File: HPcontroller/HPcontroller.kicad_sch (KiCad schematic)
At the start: 8 parts, among them J5 54-00174, U7 Adafruit_QTPY_ESP32-C3

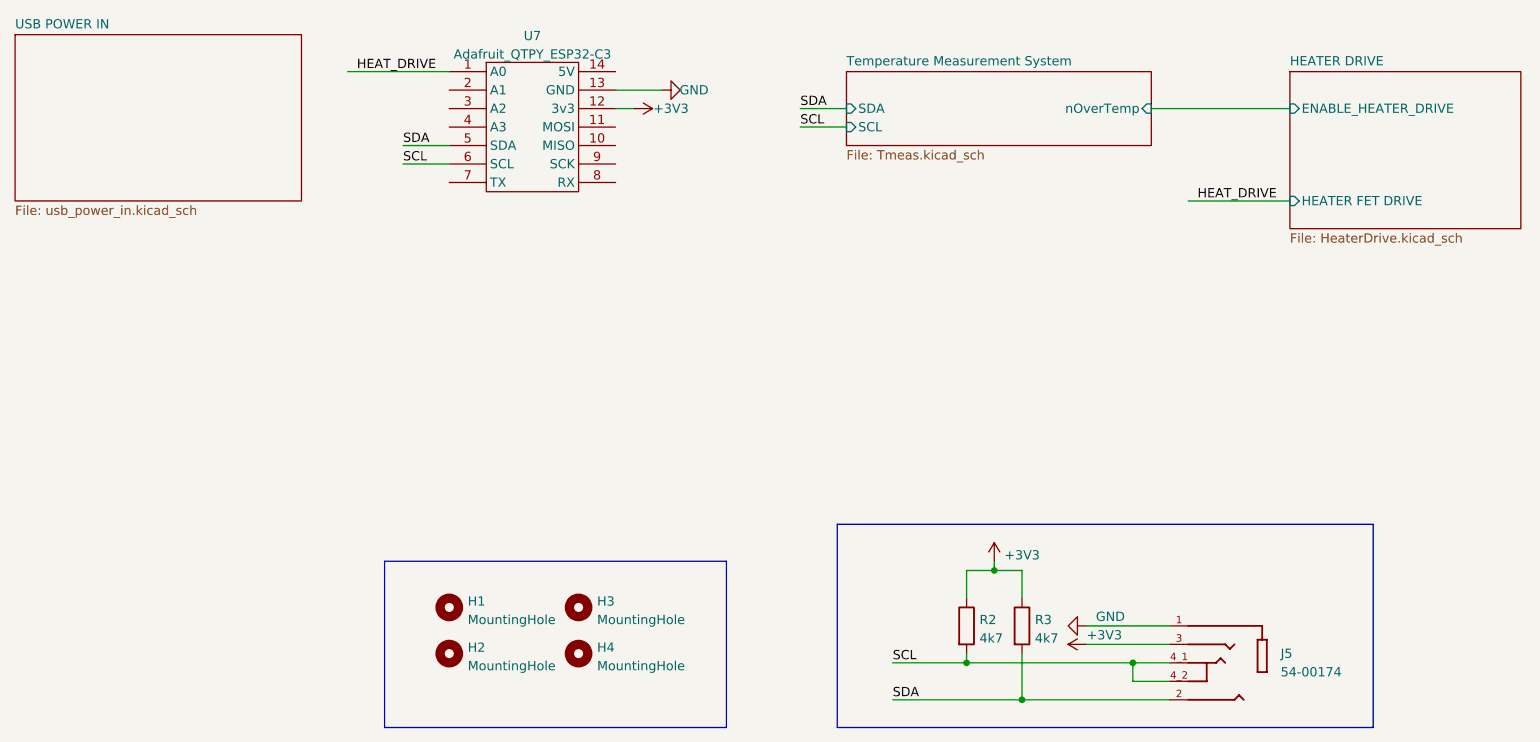
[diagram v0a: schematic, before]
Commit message: released rev c - op amp swap not fixed!
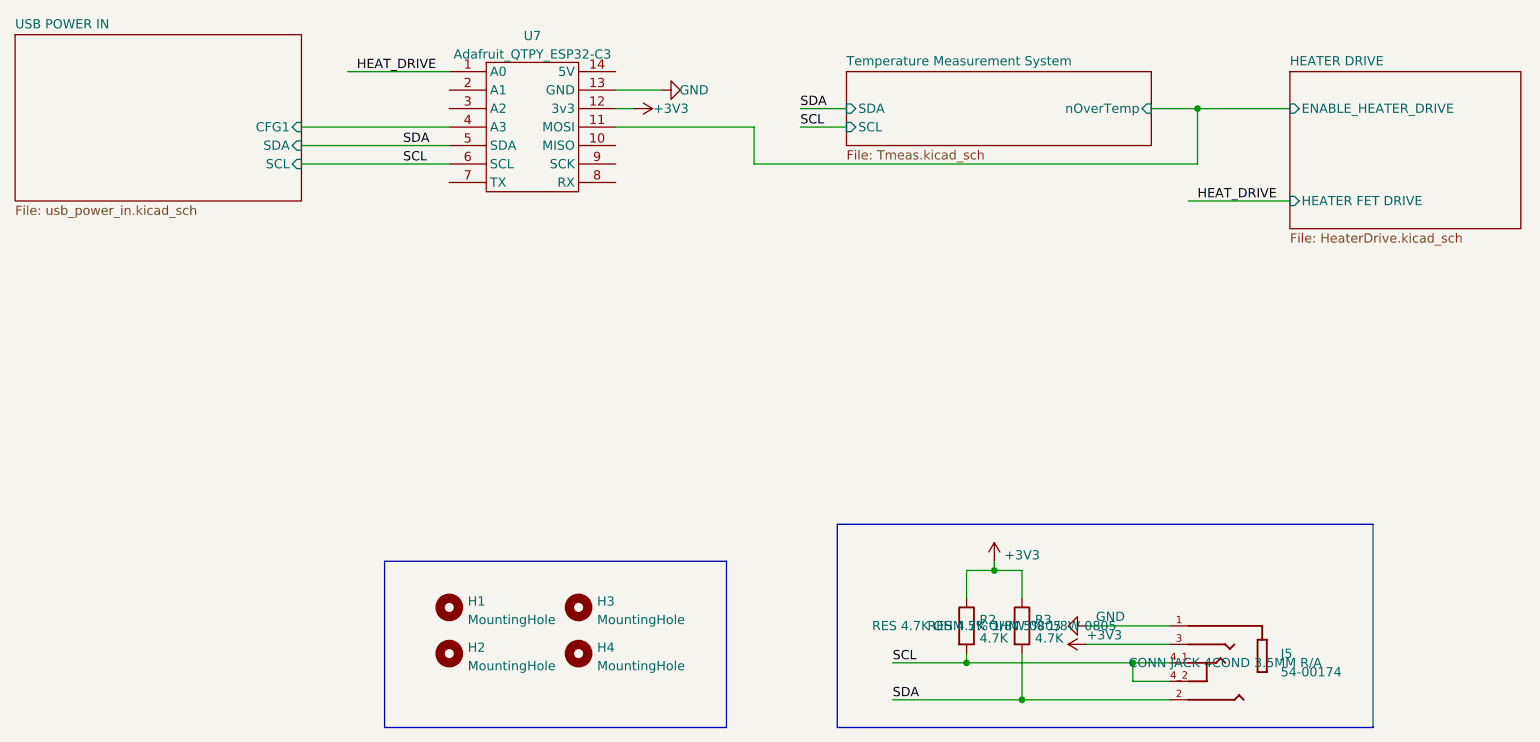
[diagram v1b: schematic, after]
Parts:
- J5: Manufacturer (none) -> Tensility International Corp; Supplier (none) -> DigiKey; Supplier_PN (none) -> 839-54-00174CT-ND
- R2, R3: value 4k7 -> 4.7K; Manufacturer (none) -> YAGEO; Package (none) -> 0805; Supplier (none) -> DigiKey; Supplier_PN (none) -> 311-4.7KARCT-ND
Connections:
- net HEATER DRIVE/ENABLE_HEATER_DRIVE: now also U7.11 (MOSI)
- net USB POWER IN/CFG1: now reaches U7.4 (A3)
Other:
- sheet USB POWER IN ports: added CFG1, SCL, SDA; removed none
